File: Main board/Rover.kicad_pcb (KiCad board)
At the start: 2 copper layers, 76.1 x 102.6 mm, 12 parts, among them J1 IN, J2 OUT, J3 Barrel_Jack_Switch, J4 MOTOR, J5 MOTOR, J6 MOTOR, J7 MOTOR, SW1 SW_DPDT_x2, U1 RASPBERRY_PI_4B_4GB

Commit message: updated pcb
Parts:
- added D1: LED, LED_THT:LED_D5.0mm_Clear, F.Cu at (178.5, 120.5)
- added J8: IMU, Connector_PinHeader_2.54mm:PinHeader_1x08_P2.54mm_Vertical, F.Cu at (207.9, 53.0)
- added REF**: mpu 6050, module:mpu 6050, F.Cu at (199.1, 59.5)
- U1: value RASPBERRY_PI_4B_4GB -> ESP32-DEVKITC-32D; footprint RASPBERRY_PI_4B_4GB:MODULE_RASPBERRY_PI_4B_4GB -> Library:MODULE_ESP32-DEVKITC-32D
- moved J1 150.2 mm to (253.0, 117.6), turned to -90 degrees
- moved REF** 135.4 mm to (235.0, 120.0), turned to 180 degrees
- moved J2 124.4 mm to (217.0, 122.5), turned to 90 degrees
- moved J7 121.3 mm to (246.5, 68.0), turned to -90 degrees
- moved J6 119.1 mm to (227.7, 68.0), turned to -90 degrees
- moved U3 109.1 mm to (235.5, 92.0), turned to -90 degrees
- moved SW1 70.5 mm to (163.6, 119.0)
- moved U1 66.4 mm to (198.7, 95.8), turned to 0 degrees
- moved J5 63.2 mm to (169.7, 68.0)
- moved J3 51.7 mm to (157.5, 120.5)
- moved U2 37.2 mm to (162.0, 92.0), turned to -90 degrees
- moved J4 34.9 mm to (150.8, 68.0)
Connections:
- U2 pad 1: PWM1 -> Net-(U1-IO32)
- U2 pad 2: IN1 1 -> Net-(U1-IO33)
- U2 pad 3: IN2 1 -> Net-(U1-IO25)
- U2 pad 4: IN3 1 -> Net-(U1-IO26)
- U2 pad 5: IN4 1 -> Net-(U1-IO27)
- U2 pad 6: PWM3 -> Net-(U1-IO14)
- U3 pad 1: PWM0 -> Net-(U1-IO19)
- U3 pad 2: IN1 2 -> Net-(U1-IO18)
- U3 pad 3: IN2 2 -> Net-(U1-IO5)
- U3 pad 4: IN3 2 -> Net-(U1-IO17)
- U3 pad 5: IN4 2 -> Net-(U1-IO16)
- U3 pad 6: PWM2 -> Net-(U1-IO4)
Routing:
- net Net-(J1-Pin_2): track 14.3 -> 106.0 mm
- net +7.4V: track 169.7 -> 235.1 mm
- net +5V: track 107.7 -> 154.5 mm
- net Net-(J6-Pin_2): track 52.6 -> 6.61 mm
- net SIG B 4: track 16.6 -> 61.9 mm
- net Net-(J6-Pin_1): track 51.6 -> 7.89 mm
- net SIG A 4: track 20.2 -> 63.6 mm
- net Net-(U1-IO33): track 0.00 -> 42.9 mm
- net Net-(U1-IO25): track 0.00 -> 42.9 mm
- net Net-(U1-IO14): track 0.00 -> 42.9 mm
- net Net-(U1-IO27): track 0.00 -> 42.9 mm
- net Net-(U1-IO26): track 0.00 -> 42.9 mm
- net Net-(U1-IO32): track 0.00 -> 42.9 mm
- net PWM1: track 40.6 -> 0.00 mm
- net Net-(J8-Pin_4): track 0.00 -> 40.3 mm
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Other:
- board size 76.1 x 102.6 mm -> 126 x 78.5 mm
- board text added: "Designed by: Ihsan"

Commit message: message
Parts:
- moved J7 155.7 mm to (90.8, 72.0), turned to 90 degrees
- moved U3 132.0 mm to (103.6, 96.2)
- moved J6 116.9 mm to (110.9, 72.0), turned to 90 degrees
- moved D1 58.6 mm to (120.1, 124.7)
- moved J3 58.6 mm to (99.1, 124.7)
- moved SW1 58.6 mm to (105.2, 123.3)
- moved J1 58.6 mm to (194.6, 121.8)
- moved J2 58.6 mm to (158.6, 126.7)
- moved J8 58.6 mm to (149.5, 57.2)
- moved REF** 58.6 mm to (140.7, 63.7)
- moved REF** 58.6 mm to (176.6, 124.2)
- moved U1 58.6 mm to (140.3, 100.0)
- moved J5 21.3 mm to (190.6, 72.0), turned to -90 degrees
- moved J4 19.2 mm to (169.7, 72.0), turned to -90 degrees
- moved U2 15.7 mm to (177.1, 96.2)
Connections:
- J4 pad 5: SIG A 1 -> MOTOR_3_ENCODER_A
- J4 pad 6: SIG B 1 -> MOTOR_3_ENCODER_B
- J5 pad 5: SIG A 2 -> MOTOR_4_ENCODER_A
- J5 pad 6: SIG B 2 -> MOTOR_4_ENCODER_B
- J6 pad 5: SIG A 3 -> MOTOR_1_ENCODER_A
- J6 pad 6: SIG B 3 -> MOTOR_1_ENCODER_B
- J7 pad 5: SIG A 4 -> MOTOR_2_ENCODER_A
- J7 pad 6: SIG B 4 -> MOTOR_2_ENCODER_B
- J8 pad 3: Net-(J8-Pin_3) -> unconnected-(J8-Pin_3-Pad3)
- J8 pad 4: Net-(J8-Pin_4) -> unconnected-(J8-Pin_4-Pad4)
- U1 pad J2-10: Net-(U1-IO26) -> MOTOR_4_PWM
- U1 pad J2-11: Net-(U1-IO27) -> MOTOR_1_DIR_FORWARD
- U1 pad J2-12: Net-(U1-IO14) -> MOTOR_1_DIR_REVERSE
- U1 pad J2-13: unconnected-(U1-IO12-PadJ2-13) -> MOTOR_2_DIR_FORWARD
- U1 pad J2-15: unconnected-(U1-IO13-PadJ2-15) -> MOTOR_2_DIR_REVERSE
- U1 pad J2-3: SIG B 2 -> MOTOR_2_ENCODER_A
- U1 pad J2-4: SIG A 2 -> MOTOR_2_ENCODER_B
- U1 pad J2-5: SIG B 1 -> unconnected-(U1-IO34-PadJ2-5)
- U1 pad J2-6: SIG A 1 -> unconnected-(U1-IO35-PadJ2-6)
- U1 pad J2-7: Net-(U1-IO32) -> MOTOR_1_PWM
- U1 pad J2-8: Net-(U1-IO33) -> MOTOR_2_PWM
- U1 pad J2-9: Net-(U1-IO25) -> MOTOR_3_PWM
- U1 pad J3-10: Net-(U1-IO5) -> MOTOR_4_ENCODER_B
- U1 pad J3-11: Net-(U1-IO17) -> MOTOR_3_DIR_FORWARD
- U1 pad J3-12: Net-(U1-IO16) -> MOTOR_3_DIR_REVERSE
- U1 pad J3-13: Net-(U1-IO4) -> MOTOR_4_DIR_FORWARD
- U1 pad J3-14: SIG B 4 -> MOTOR_4_DIR_REVERSE
- U1 pad J3-15: SIG A 4 -> unconnected-(U1-IO2-PadJ3-15)
- U1 pad J3-2: unconnected-(U1-IO23-PadJ3-2) -> MOTOR_1_ENCODER_A
- U1 pad J3-3: Net-(J8-Pin_3) -> MOTOR_1_ENCODER_B
- U1 pad J3-4: SIG B 3 -> unconnected-(U1-TXD0-PadJ3-4)
- U1 pad J3-5: SIG A 3 -> unconnected-(U1-RXD0-PadJ3-5)
- U1 pad J3-6: Net-(J8-Pin_4) -> MOTOR_3_ENCODER_A
- U1 pad J3-8: Net-(U1-IO19) -> MOTOR_3_ENCODER_B
- U1 pad J3-9: Net-(U1-IO18) -> MOTOR_4_ENCODER_A
- U2 pad 1: Net-(U1-IO32) -> MOTOR_3_PWM
- U2 pad 2: Net-(U1-IO33) -> MOTOR_3_DIR_FORWARD
- U2 pad 3: Net-(U1-IO25) -> MOTOR_3_DIR_REVERSE
- U2 pad 4: Net-(U1-IO26) -> MOTOR_4_DIR_FORWARD
- U2 pad 5: Net-(U1-IO27) -> MOTOR_4_DIR_REVERSE
- U2 pad 6: Net-(U1-IO14) -> MOTOR_4_PWM
- U3 pad 1: Net-(U1-IO19) -> MOTOR_1_PWM
- U3 pad 2: Net-(U1-IO18) -> MOTOR_1_DIR_FORWARD
- U3 pad 3: Net-(U1-IO5) -> MOTOR_1_DIR_REVERSE
- U3 pad 4: Net-(U1-IO17) -> MOTOR_2_DIR_FORWARD
- U3 pad 5: Net-(U1-IO16) -> MOTOR_2_DIR_REVERSE
- U3 pad 6: Net-(U1-IO4) -> MOTOR_2_PWM
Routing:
- net +7.4V: track 235.1 -> 0.00 mm
- net +5V: track 154.5 -> 0.00 mm
- net Net-(J1-Pin_2): track 106.0 -> 0.00 mm
- net MOTOR_2_ENCODER_B: track 0.00 -> 65.9 mm
- net SIG A 4: track 63.6 -> 0.00 mm
- net SIG B 4: track 61.9 -> 0.00 mm
- net MOTOR_4_ENCODER_B: track 0.00 -> 50.7 mm
- net MOTOR_4_ENCODER_A: track 0.00 -> 49.9 mm
- net MOTOR_2_ENCODER_A: track 0.00 -> 49.1 mm
- net MOTOR_2_PWM: track 0.00 -> 47.1 mm, vias 0 -> 1
- net MOTOR_2_DIR_REVERSE: track 0.00 -> 45.3 mm
- net MOTOR_2_DIR_FORWARD: track 0.00 -> 44.2 mm
- net MOTOR_1_DIR_REVERSE: track 0.00 -> 44.2 mm
- net MOTOR_1_DIR_FORWARD: track 0.00 -> 44.2 mm
- net Net-(U1-IO33): track 42.9 -> 0.00 mm
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
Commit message: .
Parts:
- moved J1 1.10 mm to (193.5, 121.8)
- moved REF** 0.60 mm to (176.0, 124.2)
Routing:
- net +7.4V: track 0.00 -> 321.9 mm
- net Net-(J1-Pin_2): track 0.00 -> 104.8 mm
- net MOTOR_3_PWM: track 0.00 -> 74.8 mm
- net MOTOR_4_PWM: track 0.00 -> 55.9 mm
- net Net-(D1-A): track 0.00 -> 35.5 mm, vias 0 -> 1
- net +5V: track 0.00 -> 33.3 mm
- net Net-(SW1A-B): track 0.00 -> 15.8 mm

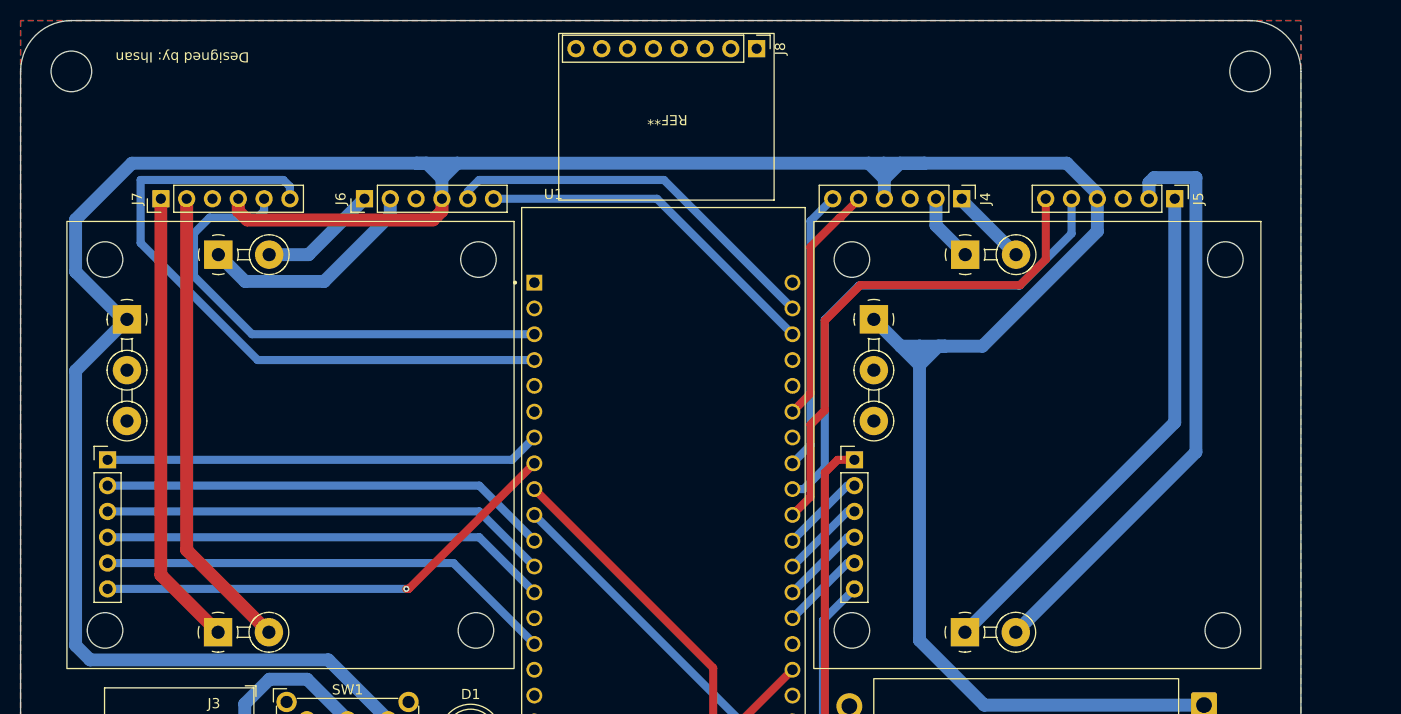
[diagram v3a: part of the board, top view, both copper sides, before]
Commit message: add edge detection
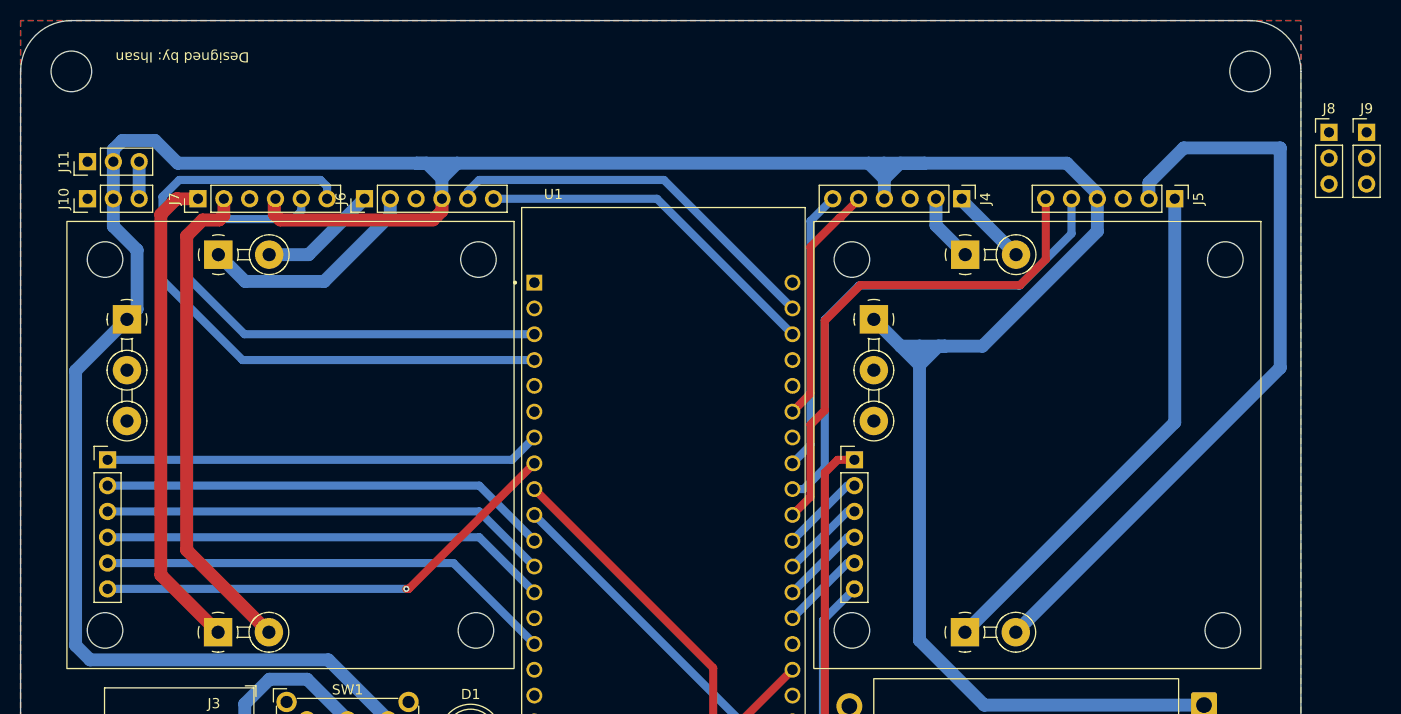
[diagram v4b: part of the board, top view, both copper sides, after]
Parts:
- removed the REF** at (140.7, 63.7)
- added J10: Servo, Connector_PinHeader_2.54mm:PinHeader_1x03_P2.54mm_Vertical, F.Cu at (83.6, 72.0)
- added J11: Servo, Connector_PinHeader_2.54mm:PinHeader_1x03_P2.54mm_Vertical, F.Cu at (83.6, 68.3)
- added J9: Servo, Connector_PinHeader_2.54mm:PinHeader_1x03_P2.54mm_Vertical, F.Cu at (209.5, 65.5)
- J8: value IMU -> Servo; footprint Connector_PinHeader_2.54mm:PinHeader_1x08_P2.54mm_Vertical -> Connector_PinHeader_2.54mm:PinHeader_1x03_P2.54mm_Vertical
- moved J8 56.9 mm to (205.8, 65.5), turned to 0 degrees
- moved J7 3.66 mm to (94.5, 72.0)
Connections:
- J8 pad 1: +5V -> GND
- J8 pad 2: GND -> +7.4V
- J8 pad 3: unconnected-(J8-Pin_3-Pad3) -> Net-(J10-Pin_3)
- U1 pad J3-15: unconnected-(U1-IO2-PadJ3-15) -> Net-(J10-Pin_3)
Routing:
- net Net-(J5-Pin_2): track 58.5 -> 74.4 mm
- net MOTOR_2_ENCODER_A: track 49.1 -> 53.9 mm
- net Net-(J10-Pin_3): track 0.00 -> 3.65 mm
- net Net-(J7-Pin_1): track 45.0 -> 47.7 mm
- net Net-(J7-Pin_2): track 46.0 -> 48.5 mm
- net +7.4V: track 321.9 -> 319.8 mm
- net MOTOR_2_ENCODER_B: track 65.9 -> 66.4 mm
